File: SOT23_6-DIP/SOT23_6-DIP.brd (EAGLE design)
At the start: 10.8 x 10.8 mm, 2 parts, among them U1 DUMMY8S

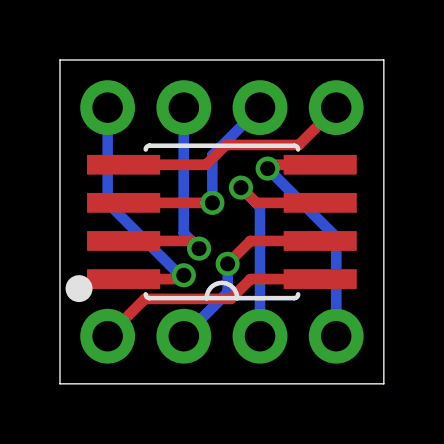
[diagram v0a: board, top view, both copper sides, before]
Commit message: sot23 + (soic8 & sot363 fix)
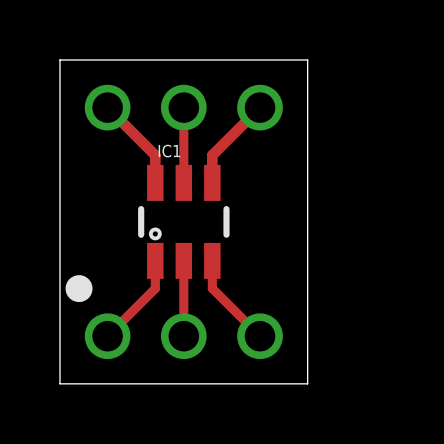
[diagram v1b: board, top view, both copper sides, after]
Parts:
- removed SOIC-8/W: ADAPTER-8, my-pinhead:ADAPTER-8
- removed U1: DUMMY8S, my-ic:SO8/W
- added IC1: MCP16251T-I/CH, my-power:SOT23-6
- added SOT23-6: ADAPTER-6, my-pinhead:ADAPTER-6
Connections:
- removed net N$7: SOIC-8/W.7, U1.7
- removed net N$8: SOIC-8/W.8, U1.8
- net N$1: now also IC1.1, SOT23-6.1; no longer SOIC-8/W.1, U1.1
- net N$2: now also IC1.2, SOT23-6.2; no longer SOIC-8/W.2, U1.2
- net N$3: now also IC1.3, SOT23-6.3; no longer SOIC-8/W.3, U1.3
- net N$4: now also IC1.6, SOT23-6.6; no longer SOIC-8/W.4, U1.4
- net N$5: now also IC1.5, SOT23-6.5; no longer SOIC-8/W.5, U1.5
- net N$6: now also IC1.4, SOT23-6.4; no longer SOIC-8/W.6, U1.6
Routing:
- net N$8: track 8.77 -> 0.00 mm, vias 1 -> 0
- net N$7: track 7.53 -> 0.00 mm, vias 1 -> 0
- net N$5: track 7.88 -> 2.51 mm
- net N$4: track 8.34 -> 3.17 mm, vias 1 -> 0
- net N$3: track 8.07 -> 3.17 mm, vias 1 -> 0
- net N$1: track 7.88 -> 3.17 mm
- net N$2: track 6.42 -> 2.51 mm, vias 1 -> 0
- net N$6: track 6.79 -> 3.17 mm, vias 1 -> 0
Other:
- board size 10.8 x 10.8 mm -> 8.3 x 10.8 mm
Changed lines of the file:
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@@
 <setting verticaltext="up"/>
 </settings>
-<grid distance="5" unitdist="mil" unit="mil" style="lines" multiple="1" display="yes" altdistance="5" altunitdist="mil" altunit="mil"/>
+<grid distance="5" unitdist="mil" unit="mil" style="lines" multiple="1" display="no" altdistance="5" altunitdist="mil" altunit="mil"/>
 <layers>
 <layer number="1" name="Top" color="4" fill="1" visible="yes" active="yes"/>
@@
 <layer number="106" name="bPlate" color="7" fill="1" visible="yes" active="yes"/>
 <layer number="107" name="Crop" color="7" fill="1" visible="yes" active="yes"/>
-<layer number="108" name="fp8" color="7" fill="1" visible="yes" active="yes"/>
-<layer number="109" name="fp9" color="7" fill="1" visible="yes" active="yes"/>
+<layer number="108" name="tplace-old" color="10" fill="1" visible="yes" active="yes"/>
+<layer number="109" name="ref-old" color="11" fill="1" visible="yes" active="yes"/>
 <layer number="110" name="fp0" color="7" fill="1" visible="yes" active="yes"/>
-<layer number="111" name="111" color="7" fill="1" visible="yes" active="yes"/>
+<layer number="111" name="LPC17xx" color="7" fill="1" visible="yes" active="yes"/>
 <layer number="112" name="tSilk" color="7" fill="1" visible="yes" active="yes"/>
-<layer number="113" name="ReferenceLS" color="7" fill="1" visible="yes" active="yes"/>
-<layer number="114" name="Badge_Outline" color="7" fill="1" visible="yes" active="yes"/>
+<layer number="113" name="IDFDebug" color="4" fill="1" visible="yes" active="yes"/>
 <layer number="115" name="115bmp" color="7" fill="1" visible="yes" active="yes"/>
 <layer number="116" name="Patch_BOT" color="9" fill="4" visible="yes" active="yes"/>
@@
 <layer number="215" name="215bmp" color="7" fill="1" visible="yes" active="yes"/>
 <layer number="216" name="216bmp" color="7" fill="1" visible="yes" active="yes"/>
-<layer number="217" name="217bmp" color="7" fill="1" visible="yes" active="yes"/>
-<layer number="218" name="218bmp" color="7" fill="1" visible="yes" active="yes"/>
-<layer number="219" name="219bmp" color="7" fill="1" visible="yes" active="yes"/>
-<layer number="220" name="220bmp" color="7" fill="1" visible="yes" active="yes"/>
-<layer number="221" name="221bmp" color="7" fill="1" visible="yes" active="yes"/>
-<layer number="222" name="222bmp" color="7" fill="1" visible="yes" active="yes"/>
-<layer number="223" name="223bmp" color="7" fill="1" visible="yes" active="yes"/>
-<layer number="224" name="224bmp" color="7" fill="1" visible="yes" active="yes"/>
+<layer number="217" name="217bmp" color="18" fill="1" visible="no" active="no"/>
+<layer number="218" name="218bmp" color="19" fill="1" visible="no" active="no"/>
+<layer number="219" name="219bmp" color="20" fill="1" visible="no" active="no"/>
+<layer number="220" name="220bmp" color="21" fill="1" visible="no" active="no"/>
+<layer number="221" name="221bmp" color="22" fill="1" visible="no" active="no"/>
+<layer number="222" name="222bmp" color="23" fill="1" visible="no" active="no"/>
+<layer number="223" name="223bmp" color="24" fill="1" visible="no" active="no"/>
+<layer number="224" name="224bmp" color="25" fill="1" visible="no" active="no"/>
 <layer number="225" name="225bmp" color="7" fill="1" visible="yes" active="yes"/>
 <layer number="226" name="226bmp" color="7" fill="1" visible="yes" active="yes"/>
@@
 <board>
 <plain>
-<wire x1="0" y1="0" x2="0" y2="10.795" width="0" layer="20"/>
-<wire x1="0" y1="10.795" x2="10.795" y2="10.795" width="0" layer="20"/>
-<wire x1="10.795" y1="10.795" x2="10.795" y2="0" width="0" layer="20"/>
-<wire x1="10.795" y1="0" x2="0" y2="0" width="0" layer="20"/>
+<wire x1="0" y1="0" x2="8.255" y2="0" width="0" layer="20"/>
+<wire x1="8.255" y1="0" x2="8.255" y2="10.795" width="0" layer="20"/>
+<wire x1="8.255" y1="10.795" x2="0" y2="10.795" width="0" layer="20"/>
+<wire x1="0" y1="10.795" x2="0" y2="0" width="0" layer="20"/>
 </plain>
 <attributes>
@@
 <param name="rvMicroViaOuter" value="0.25"/>
 <param name="rvMicroViaInner" value="0.25"/>
-<param name="rlMinPadTop" value="16mil"/>
+<param name="rlMinPadTop" value="1mil"/>
 <param name="rlMaxPadTop" value="20mil"/>
 <param name="rlMinPadInner" value="16mil"/>
@@
 </autorouter>
 <elements>
-<element name="SOIC-8/W" library="my-pinhead" package="ADAPTER-8" value="ADAPTER-8" x="0" y="0"/>
-<element name="U1" library="my-ic" package="SO8/W" value="DUMMY8S" x="5.3975" y="5.3975" smashed="yes" rot="R90"/>
+<element name="SOT23-6" library="my-pinhead" package="ADAPTER-6" value="ADAPTER-6" x="0" y="0"/>
+<element name="IC1" library="my-power" package="SOT23-6" value="MCP16251T-I/CH" x="4.1275" y="5.3975">
+<attribute name="ATTR" value="True disconnect" x="4.1275" y="5.3975" size="1.778" layer="27" display="off"/>
+</element>
 </elements>
 <signals>
 <signal name="N$1">
-<contactref element="U1" pad="1"/>
-<contactref element="SOIC-8/W" pad="1"/>
-<wire x1="6.35" y1="3.4925" x2="8.6741" y2="3.4925" width="0.3556" layer="1"/>
-<wire x1="1.5875" y1="1.5875" x2="2.8321" y2="2.8321" width="0.3556" layer="1"/>
-<wire x1="2.8321" y1="2.8321" x2="5.6896" y2="2.8321" width="0.3556" layer="1"/>
-<wire x1="5.6896" y1="2.8321" x2="6.35" y2="3.4925" width="0.3556" layer="1"/>
+<contactref element="IC1" pad="1"/>
+<contactref element="SOT23-6" pad="1"/>
+<wire x1="3.1775" y1="4.0974" x2="3.1775" y2="3.1775" width="0.3048" layer="1"/>
+<wire x1="3.1775" y1="3.1775" x2="1.5875" y2="1.5875" width="0.3048" layer="1"/>
 </signal>
 <signal name="N$2">
-<contactref element="U1" pad="2"/>
-<contactref element="SOIC-8/W" pad="2"/>
-<via x="5.588" y="4.0005" extent="1-16" drill="0.5"/>
-<wire x1="4.1275" y1="1.5875" x2="5.588" y2="3.048" width="0.3556" layer="16"/>
-<wire x1="5.588" y1="3.048" x2="5.588" y2="4.0005" width="0.3556" layer="16"/>
-<wire x1="8.6741" y1="4.7625" x2="6.35" y2="4.7625" width="0.3556" layer="1"/>
-<wire x1="6.35" y1="4.7625" x2="5.588" y2="4.0005" width="0.3556" layer="1"/>
+<contactref element="SOT23-6" pad="2"/>
+<contactref element="IC1" pad="2"/>
+<wire x1="4.1275" y1="1.5875" x2="4.1275" y2="4.0974" width="0.3048" layer="1"/>
 </signal>
 <signal name="N$3">
-<contactref element="U1" pad="3"/>
-<contactref element="SOIC-8/W" pad="3"/>
-<via x="6.0325" y="6.5405" extent="1-16" drill="0.5"/>
-<wire x1="6.6675" y1="1.5875" x2="6.6675" y2="5.9055" width="0.3556" layer="16"/>
-<wire x1="6.6675" y1="5.9055" x2="6.0325" y2="6.5405" width="0.3556" layer="16"/>
-<wire x1="6.0325" y1="6.5405" x2="6.5405" y2="6.0325" width="0.3556" layer="1"/>
-<wire x1="6.5405" y1="6.0325" x2="8.6741" y2="6.0325" width="0.3556" layer="1"/>
+<contactref element="SOT23-6" pad="3"/>
+<contactref element="IC1" pad="3"/>
+<wire x1="5.0775" y1="4.0974" x2="5.0775" y2="3.1775" width="0.3048" layer="1"/>
+<wire x1="5.0775" y1="3.1775" x2="6.6675" y2="1.5875" width="0.3048" layer="1"/>
 </signal>
 <signal name="N$4">
-<contactref element="U1" pad="4"/>
-<contactref element="SOIC-8/W" pad="4"/>
-<via x="6.9215" y="7.1755" extent="1-16" drill="0.5"/>
-<wire x1="8.6741" y1="7.3025" x2="7.0485" y2="7.3025" width="0.3556" layer="1"/>
-<wire x1="7.0485" y1="7.3025" x2="6.9215" y2="7.1755" width="0.3556" layer="1"/>
-<wire x1="6.9215" y1="7.1755" x2="9.2075" y2="4.8895" width="0.3556" layer="16"/>
-<wire x1="9.2075" y1="4.8895" x2="9.2075" y2="1.5875" width="0.3556" layer="16"/>
+<contactref element="IC1" pad="6"/>
+<contactref element="SOT23-6" pad="6"/>
+<wire x1="1.5875" y1="9.2075" x2="3.1775" y2="7.6175" width="0.3556" layer="1"/>
+<wire x1="3.1775" y1="7.6175" x2="3.1775" y2="6.6976" width="0.3556" layer="1"/>
 </signal>
 <signal name="N$5">
-<contactref element="U1" pad="5"/>
-<contactref element="SOIC-8/W" pad="5"/>
-<wire x1="9.2075" y1="9.2075" x2="7.9629" y2="7.9629" width="0.3556" layer="1"/>
-<wire x1="7.9629" y1="7.9629" x2="5.52984375" y2="7.9629" width="0.3556" layer="1"/>
-<wire x1="5.52984375" y1="7.9629" x2="4.86944375" y2="7.3025" width="0.3556" layer="1"/>
-<wire x1="4.86944375" y1="7.3025" x2="2.1209" y2="7.3025" width="0.3556" layer="1"/>
+<contactref element="SOT23-6" pad="5"/>
+<contactref element="IC1" pad="5"/>
+<wire x1="4.1275" y1="6.6976" x2="4.1275" y2="9.2075" width="0.3048" layer="1"/>
 </signal>
 <signal name="N$6">
-<contactref element="SOIC-8/W" pad="6"/>
-<contactref element="U1" pad="6"/>
-<wire x1="2.1209" y1="6.0325" x2="5.08" y2="6.0325" width="0.3556" layer="1"/>
-<via x="5.08" y="6.0325" extent="1-16" drill="0.5"/>
-<wire x1="6.6675" y1="9.2075" x2="5.08" y2="7.62" width="0.3556" layer="16"/>
-<wire x1="5.08" y1="7.62" x2="5.08" y2="6.0325" width="0.3556" layer="16"/>
-</signal>
-<signal name="N$7">
-<contactref element="U1" pad="7"/>
-<contactref element="SOIC-8/W" pad="7"/>
-<via x="4.6355" y="4.5085" extent="1-16" drill="0.5"/>
-<wire x1="2.1209" y1="4.7625" x2="4.3815" y2="4.7625" width="0.3556" layer="1"/>
-<wire x1="4.3815" y1="4.7625" x2="4.6355" y2="4.5085" width="0.3556" layer="1"/>
-<wire x1="4.1275" y1="9.2075" x2="4.1275" y2="5.0165" width="0.3556" layer="16"/>
-<wire x1="4.1275" y1="5.0165" x2="4.6355" y2="4.5085" width="0.3556" layer="16"/>
-</signal>
-<signal name="N$8">
-<contactref element="SOIC-8/W" pad="8"/>
-<contactref element="U1" pad="8"/>
-<via x="4.1275" y="3.6195" extent="1-16" drill="0.5"/>
-<wire x1="1.5875" y1="9.2075" x2="1.5875" y2="6.0325" width="0.3556" layer="16"/>
-<wire x1="2.1209" y1="3.4925" x2="4.0005" y2="3.4925" width="0.3556" layer="1"/>
-<wire x1="4.0005" y1="3.4925" x2="4.1275" y2="3.6195" width="0.3556" layer="1"/>
-<wire x1="1.5875" y1="6.0325" x2="4.0005" y2="3.6195" width="0.3556" layer="16"/>
-<wire x1="4.0005" y1="3.6195" x2="4.1275" y2="3.6195" width="0.3556" layer="16"/>
+<contactref element="IC1" pad="4"/>
+<contactref element="SOT23-6" pad="4"/>
+<wire x1="6.6675" y1="9.2075" x2="5.0775" y2="7.6175" width="0.3556" layer="1"/>
+<wire x1="5.0775" y1="7.6175" x2="5.0775" y2="6.6976" width="0.3556" layer="1"/>
 </signal>
 </signals>
